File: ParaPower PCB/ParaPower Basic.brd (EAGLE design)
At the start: 144.8 x 106.7 mm, 4 parts, among them U1 ESP32_ESP-WROOM-32

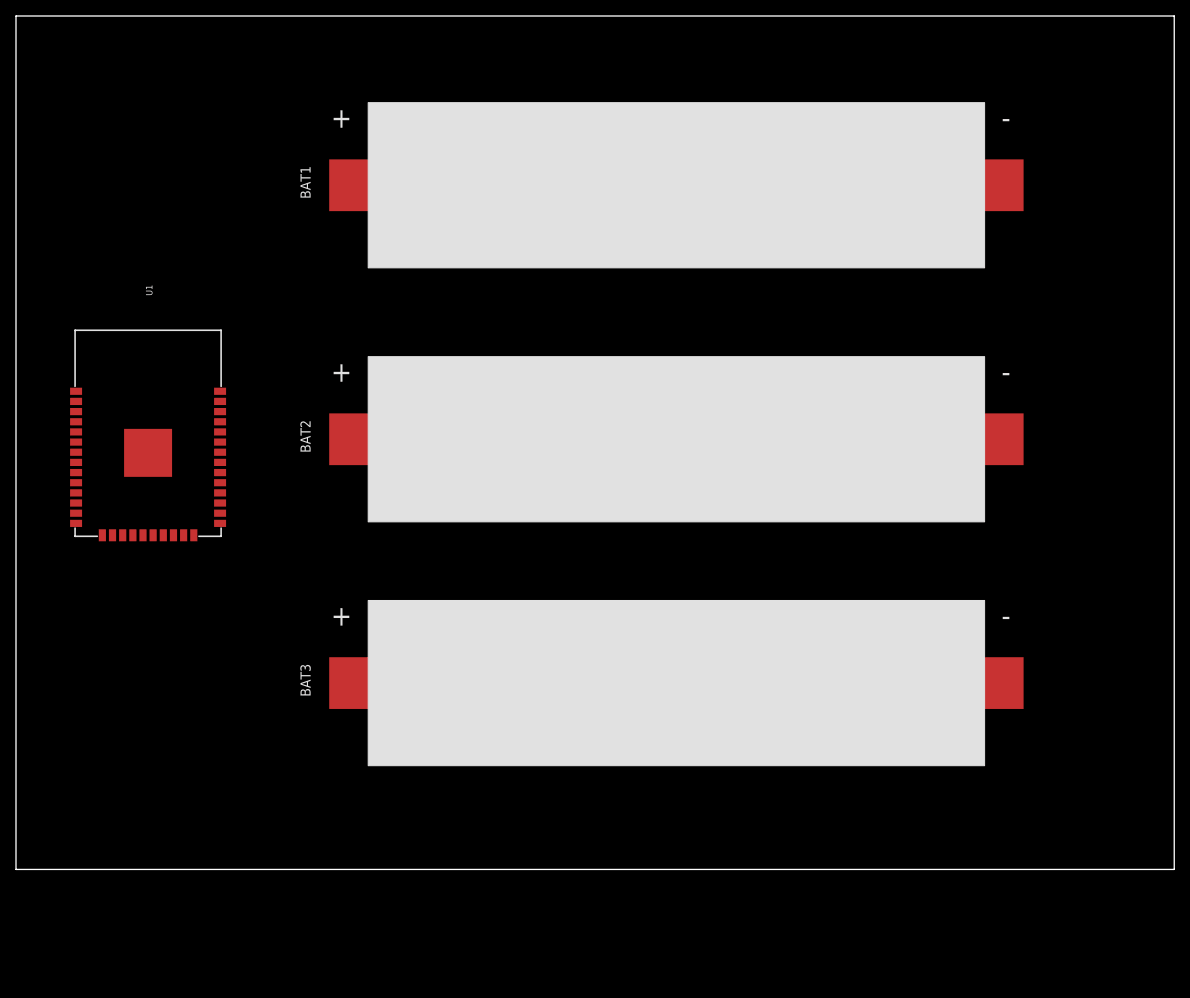
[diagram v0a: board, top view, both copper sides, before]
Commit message: started to add voltage regulation section
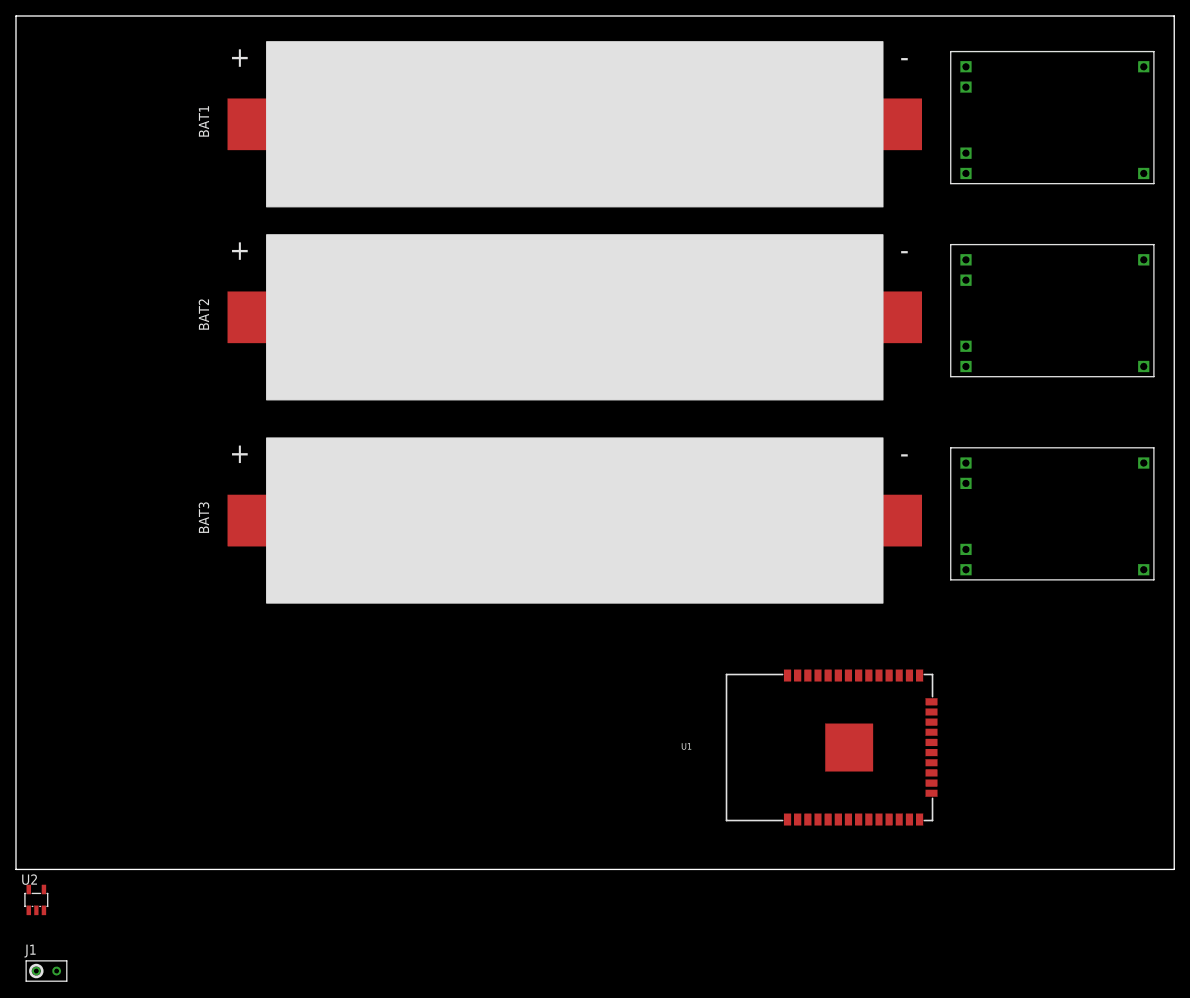
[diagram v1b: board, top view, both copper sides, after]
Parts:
- added J1: POWER-VIAS, VanEagleLib:2CT-VIAS
- added U$1, U$2, U$3: TP4056-MODULE, userlib:TP4056-LITHIUM-PROTECTED-MODULE
- added U2: TPS736, VanEagleLib:SOT23-5L
- moved U1 95.1 mm to (104.1, 15.2), turned to 180 degrees
- moved BAT3 24.0 mm to (69.8, 38.1)
- moved BAT2 19.8 mm to (69.8, 63.5)
- moved BAT1 14.8 mm to (69.8, 87.6)
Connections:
- new net +5V: J1.1
- new net 3V3: U1.2, U2.5
- new net B+: U$1.B+, U$2.B+, U$3.B+
- new net B-: U$1.B-, U$2.B-, U$3.B-
- new net GND: J1.2, U1.1, U2.2
- new net IN: U2.1
- new net IN+: U$1.IN+, U$2.IN+, U$3.IN+
- new net IN-: U$1.IN-, U$2.IN-, U$3.IN-
- new net OUT+: U$1.OUT+, U$2.OUT+, U$3.OUT+
- new net OUT-: U$1.OUT-, U$2.OUT-, U$3.OUT-
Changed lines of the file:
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@@
 </autorouter>
 <elements>
-<element name="BAT1" library="VanEagleLib" library_urn="urn:adsk.eagle:library:5408729" package="KEYSTONE_1042" package3d_urn="urn:adsk.eagle:package:8894325/1" value="KEYSTONE-1042" x="82.55" y="80.01" smashed="yes">
-<attribute name="NAME" x="36.83" y="83.82" size="1.27" layer="25" rot="R90"/>
+<element name="BAT1" library="VanEagleLib" library_urn="urn:adsk.eagle:library:5408729" package="KEYSTONE_1042" package3d_urn="urn:adsk.eagle:package:8894325/1" value="KEYSTONE-1042" x="69.85" y="87.63" smashed="yes">
+<attribute name="NAME" x="24.13" y="91.44" size="1.27" layer="25" rot="R90"/>
 </element>
-<element name="BAT2" library="VanEagleLib" library_urn="urn:adsk.eagle:library:5408729" package="KEYSTONE_1042" package3d_urn="urn:adsk.eagle:package:8894325/1" value="KEYSTONE-1042" x="82.55" y="48.26" smashed="yes">
-<attribute name="NAME" x="36.83" y="52.07" size="1.27" layer="25" rot="R90"/>
+<element name="BAT2" library="VanEagleLib" library_urn="urn:adsk.eagle:library:5408729" package="KEYSTONE_1042" package3d_urn="urn:adsk.eagle:package:8894325/1" value="KEYSTONE-1042" x="69.85" y="63.5" smashed="yes">
+<attribute name="NAME" x="24.13" y="67.31" size="1.27" layer="25" rot="R90"/>
 </element>
-<element name="BAT3" library="VanEagleLib" library_urn="urn:adsk.eagle:library:5408729" package="KEYSTONE_1042" package3d_urn="urn:adsk.eagle:package:8894325/1" value="KEYSTONE-1042" x="82.55" y="17.78" smashed="yes">
-<attribute name="NAME" x="36.83" y="21.59" size="1.27" layer="25" rot="R90"/>
+<element name="BAT3" library="VanEagleLib" library_urn="urn:adsk.eagle:library:5408729" package="KEYSTONE_1042" package3d_urn="urn:adsk.eagle:package:8894325/1" value="KEYSTONE-1042" x="69.85" y="38.1" smashed="yes">
+<attribute name="NAME" x="24.13" y="41.91" size="1.27" layer="25" rot="R90"/>
 </element>
-<element name="U1" library="VCO - Pod Daughterboard v2.0" package="ESP32_ESP-WROOM-32" value="ESP32_ESP-WROOM-32" x="16.51" y="52.07" smashed="yes" rot="R90">
-<attribute name="NAME" x="16.65" y="72.39" size="0.8128" layer="25" rot="R270" align="center"/>
-<attribute name="VALUE" x="16.51" y="45.58" size="0.8128" layer="27" rot="R180" align="center"/>
+<element name="U1" library="VCO - Pod Daughterboard v2.0" package="ESP32_ESP-WROOM-32" value="ESP32_ESP-WROOM-32" x="104.14" y="15.24" smashed="yes" rot="R180">
+<attribute name="NAME" x="83.82" y="15.38" size="0.8128" layer="25" align="center"/>
+<attribute name="VALUE" x="110.63" y="15.24" size="0.8128" layer="27" rot="R270" align="center"/>
+</element>
+<element name="U$1" library="userlib" package="TP4056-LITHIUM-PROTECTED-MODULE" value="TP4056-MODULE" x="129.54" y="93.98" smashed="yes" rot="R180"/>
+<element name="U$2" library="userlib" package="TP4056-LITHIUM-PROTECTED-MODULE" value="TP4056-MODULE" x="129.54" y="69.85" smashed="yes" rot="R180"/>
+<element name="U$3" library="userlib" package="TP4056-LITHIUM-PROTECTED-MODULE" value="TP4056-MODULE" x="129.54" y="44.45" smashed="yes" rot="R180"/>
+<element name="U2" library="VanEagleLib" library_urn="urn:adsk.eagle:library:5408729" package="SOT23-5L" package3d_urn="urn:adsk.eagle:package:8894413/1" value="TPS736" x="2.54" y="-3.81" smashed="yes">
+<attribute name="NAME" x="0.635" y="-1.905" size="1.27" layer="25"/>
+<attribute name="VALUE" x="0.635" y="-7.239" size="1.27" layer="27"/>
+</element>
+<element name="J1" library="VanEagleLib" library_urn="urn:adsk.eagle:library:5408729" package="2CT-VIAS" package3d_urn="urn:adsk.eagle:package:7547424/1" value="POWER-VIAS" x="3.81" y="-13.97" smashed="yes">
+<attribute name="NAME" x="1.143" y="-10.668" size="1.27" layer="25"/>
+<attribute name="VALUE" x="1.143" y="-16.002" size="1.27" layer="27"/>
 </element>
 </elements>
@@
 <contactref element="BAT2" pad="1"/>
 <contactref element="BAT3" pad="1"/>
-<wire x1="42.88" y1="53.774" x2="42.88" y2="85.524" width="0" layer="19" extent="1-1"/>
-<wire x1="42.88" y1="23.294" x2="42.88" y2="53.774" width="0" layer="19" extent="1-1"/>
+<wire x1="30.18" y1="69.014" x2="30.18" y2="93.144" width="0" layer="19" extent="1-1"/>
+<wire x1="30.18" y1="43.614" x2="30.18" y2="69.014" width="0" layer="19" extent="1-1"/>
 </signal>
 <signal name="-">
@@
 <contactref element="BAT2" pad="2"/>
 <contactref element="BAT3" pad="2"/>
-<wire x1="122.22" y1="53.774" x2="122.22" y2="23.294" width="0" layer="19" extent="1-1"/>
-<wire x1="122.22" y1="85.524" x2="122.22" y2="53.774" width="0" layer="19" extent="1-1"/>
+<wire x1="109.52" y1="69.014" x2="109.52" y2="43.614" width="0" layer="19" extent="1-1"/>
+<wire x1="109.52" y1="93.144" x2="109.52" y2="69.014" width="0" layer="19" extent="1-1"/>
+</signal>
+<signal name="IN+">
+<contactref element="U$1" pad="IN+"/>
+<contactref element="U$2" pad="IN+"/>
+<contactref element="U$3" pad="IN+"/>
+<wire x1="140.97" y1="62.865" x2="140.97" y2="37.465" width="0" layer="19" extent="1-1"/>
+<wire x1="140.97" y1="86.995" x2="140.97" y2="62.865" width="0" layer="19" extent="1-1"/>
+</signal>
+<signal name="IN-">
+<contactref element="U$1" pad="IN-"/>
+<contactref element="U$2" pad="IN-"/>
+<contactref element="U$3" pad="IN-"/>
+<wire x1="140.97" y1="76.2" x2="140.97" y2="50.8" width="0" layer="19" extent="1-1"/>
+<wire x1="140.97" y1="100.33" x2="140.97" y2="76.2" width="0" layer="19" extent="1-1"/>
+</signal>
+<signal name="OUT+">
+<contactref element="U$1" pad="OUT+"/>
+<contactref element="U$2" pad="OUT+"/>
+<contactref element="U$3" pad="OUT+"/>
+<wire x1="118.745" y1="62.865" x2="118.745" y2="86.995" width="0" layer="19" extent="1-1"/>
+<wire x1="118.745" y1="37.465" x2="118.745" y2="62.865" width="0" layer="19" extent="1-1"/>
+</signal>
+<signal name="B+">
+<contactref element="U$1" pad="B+"/>
+<contactref element="U$2" pad="B+"/>
+<contactref element="U$3" pad="B+"/>
+<wire x1="118.745" y1="65.405" x2="118.745" y2="89.535" width="0" layer="19" extent="1-1"/>
+<wire x1="118.745" y1="40.005" x2="118.745" y2="65.405" width="0" layer="19" extent="1-1"/>
+</signal>
+<signal name="B-">
+<contactref element="U$1" pad="B-"/>
+<contactref element="U$2" pad="B-"/>
+<contactref element="U$3" pad="B-"/>
+<wire x1="118.745" y1="73.66" x2="118.745" y2="48.26" width="0" layer="19" extent="1-1"/>
+<wire x1="118.745" y1="97.79" x2="118.745" y2="73.66" width="0" layer="19" extent="1-1"/>
+</signal>
+<signal name="OUT-">
+<contactref element="U$1" pad="OUT-"/>
+<contactref element="U$2" pad="OUT-"/>
+<contactref element="U$3" pad="OUT-"/>
+<wire x1="118.745" y1="76.2" x2="118.745" y2="50.8" width="0" layer="19" extent="1-1"/>
+<wire x1="118.745" y1="100.33" x2="118.745" y2="76.2" width="0" layer="19" extent="1-1"/>
+</signal>
+<signal name="IN">
+<contactref element="U2" pad="1"/>
+</signal>
+<signal name="GND">
+<contactref element="U2" pad="2"/>
+<contactref element="J1" pad="2"/>
+<contactref element="U1" pad="1"/>
+<wire x1="5.08" y1="-12.7" x2="96.44" y2="6.24" width="0" layer="19" extent="1-1"/>
+<wire x1="2.54" y1="-5.11" x2="5.08" y2="-12.7" width="0" layer="19" extent="1-1"/>
+</signal>
+<signal name="+5V">
+<contactref element="J1" pad="1"/>
+</signal>
+<signal name="3V3">
+<contactref element="U1" pad="2"/>
+<contactref element="U2" pad="5"/>
+<wire x1="1.59" y1="-2.51" x2="97.71" y2="6.24" width="0" layer="19" extent="1-1"/>
 </signal>
 </signals>
